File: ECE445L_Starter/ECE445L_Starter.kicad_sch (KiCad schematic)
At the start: 20 parts, among them J101 EXT_3V3, Q101 IRLD024PBF, SW101 UP, SW102 DOWN, SW103 LEFT, SW104 RIGHT, SW105 MODE, U101 EK-TM4C123GXL, U102 ESP8266-1, U103 Adafruit ST7735R

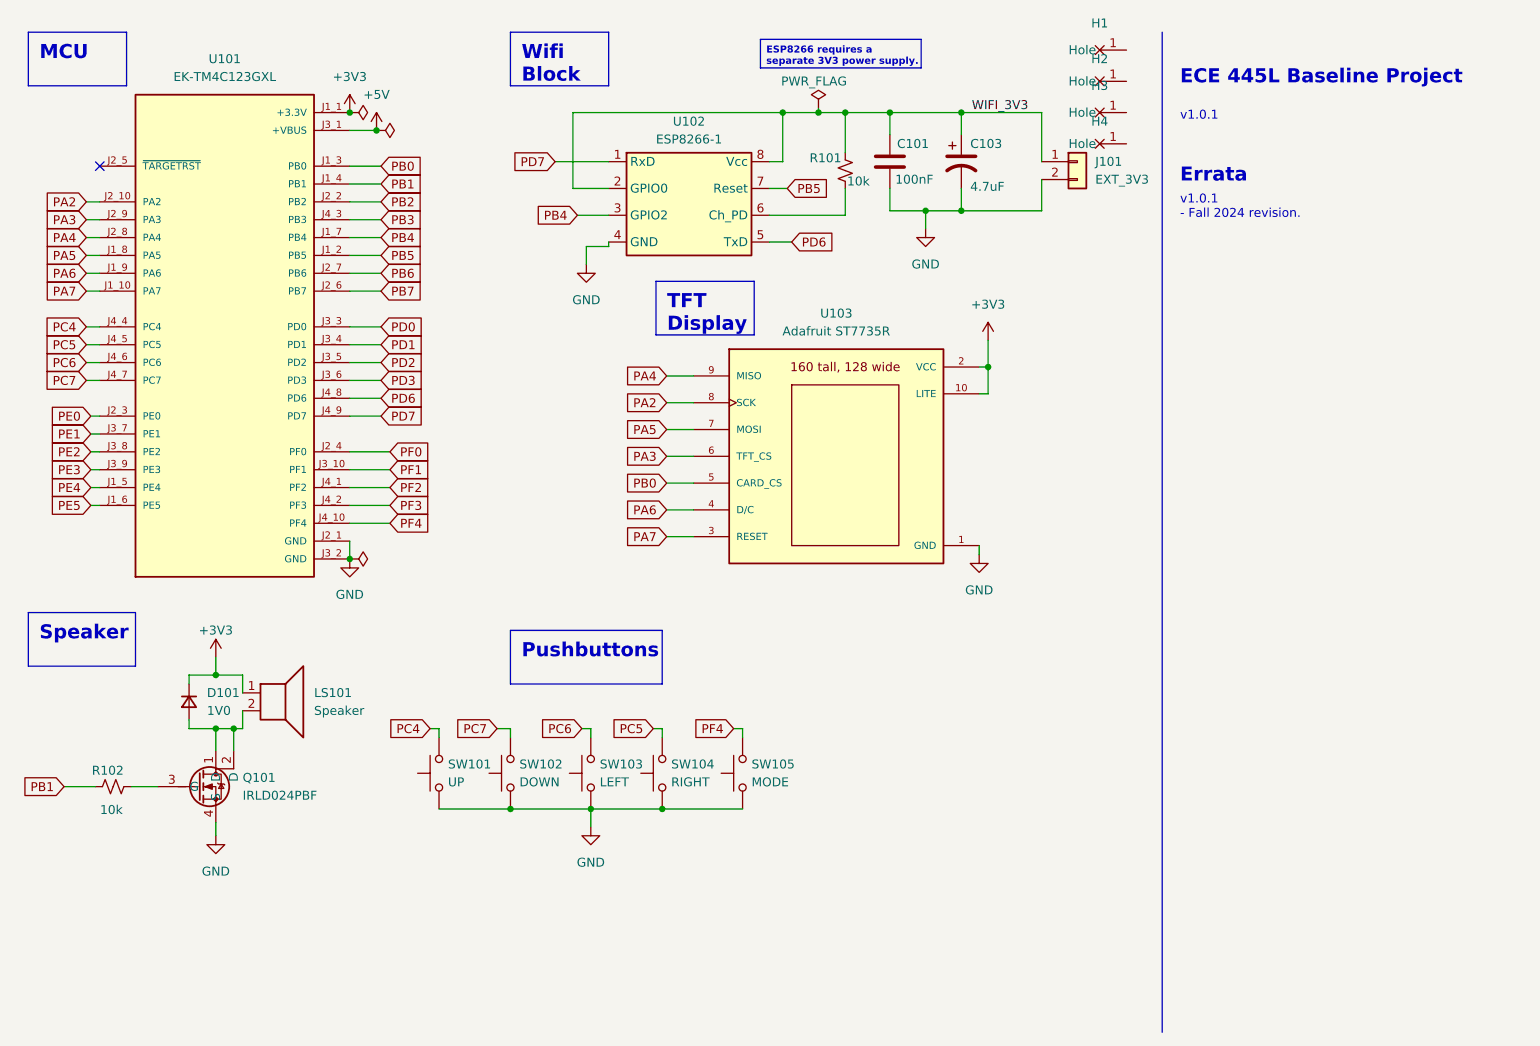
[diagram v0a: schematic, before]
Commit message: update all symbols and re-sync footprints in the KiCad projects
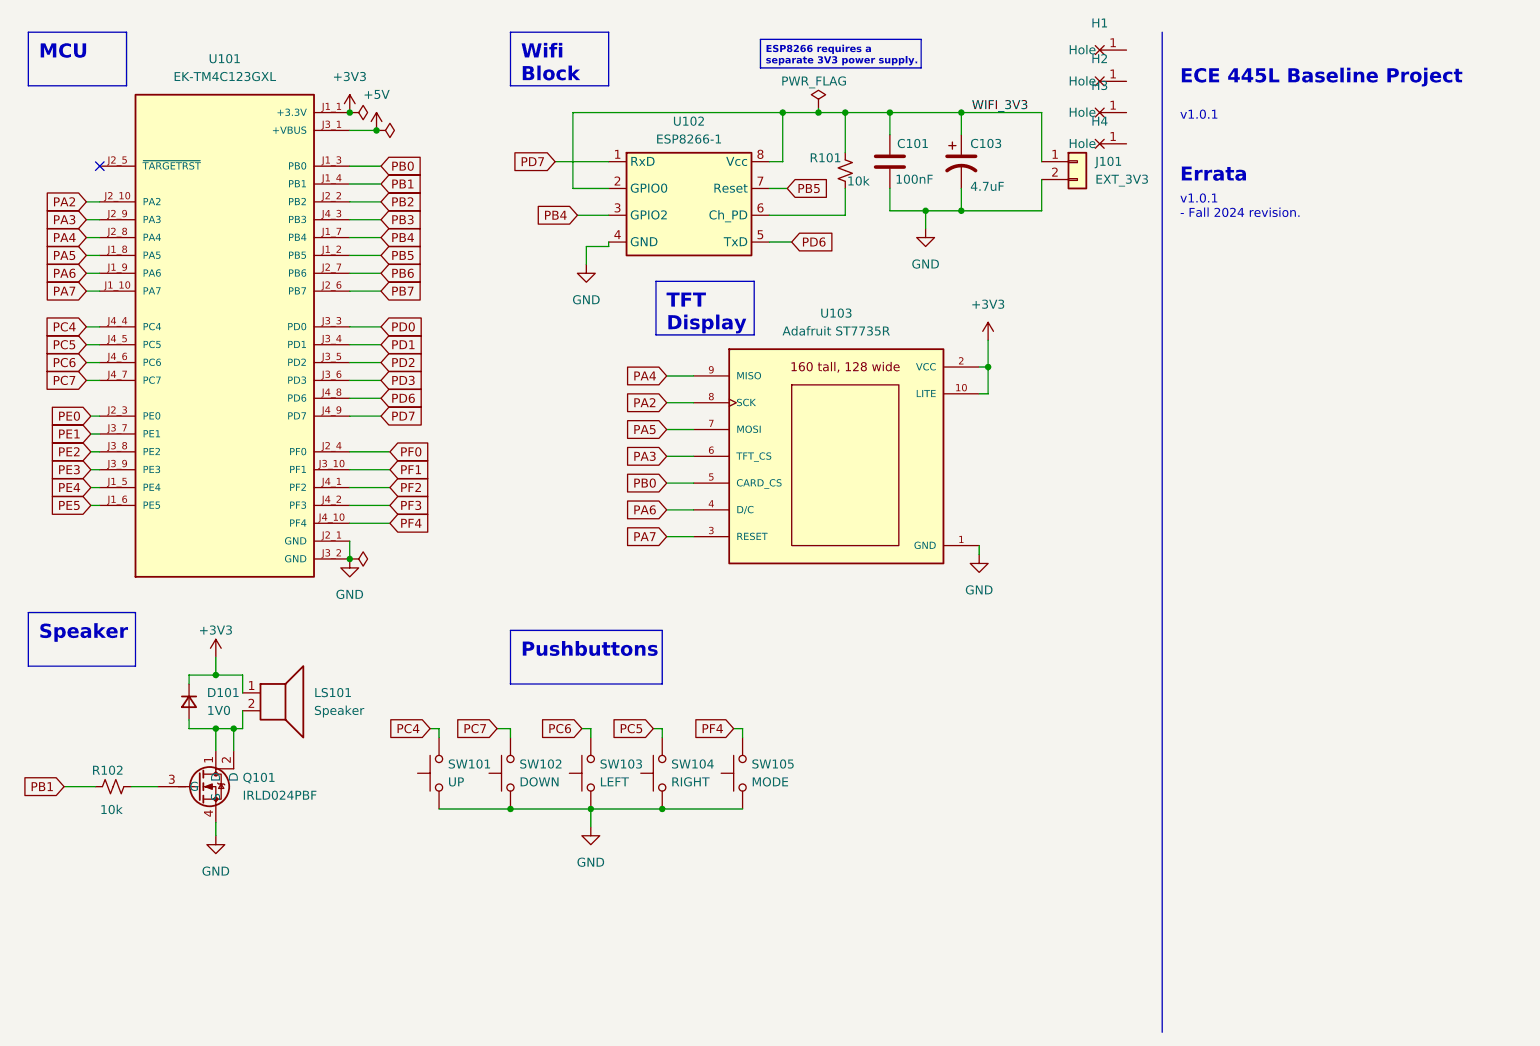
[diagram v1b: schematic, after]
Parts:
- U102: footprint ECE445L:PinHeader_2x04_P2.54mm_Vertical -> ECE445L:ESP8266_FemaleConnector
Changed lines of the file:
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@@
 (kicad_sch
-	(version 20231120)
+	(version 20250114)
 	(generator "eeschema")
-	(generator_version "8.0")
+	(generator_version "9.0")
 	(paper "A4")
 	(title_block
@@
 		(company "The University of Texas at Austin")
 	)
+	(text "v1.0.1\n- Fall 2024 revision."
+		(exclude_from_sim no)
+		(at 179.07 41.91 0)
+		(effects
+			(font
+				(size 1.27 1.27)
+			)
+			(justify left bottom)
+		)
+	)
+	(text "ECE 445L Baseline Project"
+		(exclude_from_sim no)
+		(at 179.07 22.86 0)
+		(effects
+			(font
+				(size 2 2)
+				(thickness 0.6)
+				(bold yes)
+			)
+			(justify left bottom)
+		)
+	)
+	(text "v1.0.1"
+		(exclude_from_sim no)
+		(at 179.07 27.94 0)
+		(effects
+			(font
+				(size 1.27 1.27)
+			)
+			(justify left bottom)
+		)
+	)
+	(text "Errata"
+		(exclude_from_sim no)
+		(at 179.07 36.83 0)
+		(effects
+			(font
+				(size 2 2)
+				(thickness 0.4)
+				(bold yes)
+			)
+			(justify left bottom)
+		)
+	)
+	(text_box "MCU"
+		(exclude_from_sim no)
+		(at 15.24 15.24 0)
+		(size 13.97 7.62)
+		(margins 1.5 1.5 1.5 1.5)
+		(stroke
+			(width 0)
+			(type default)
+		)
+		(fill
+			(type none)
+		)
+		(effects
+			(font
+				(size 2 2)
+				(thickness 0.4)
+				(bold yes)
+			)
+			(justify left top)
+		)
+	)
+	(text_box "ESP8266 requires a separate 3V3 power supply."
+		(exclude_from_sim no)
+		(at 119.38 16.256 0)
+		(size 22.86 4.064)
+		(margins 0.75 0.75 0.75 0.75)
+		(stroke
+			(width 0)
+			(type default)
+		)
+		(fill
+			(type none)
+		)
+		(effects
+			(font
+				(size 1 1)
+				(bold yes)
+			)
+			(justify left top)
+		)
+	)
+	(text_box "Speaker"
+		(exclude_from_sim no)
+		(at 15.24 97.79 0)
+		(size 15.24 7.62)
+		(margins 1.5 1.5 1.5 1.5)
+		(stroke
+			(width 0)
+			(type default)
+		)
+		(fill
+			(type none)
+		)
+		(effects
+			(font
+				(size 2 2)
+				(thickness 0.4)
+				(bold yes)
+			)
+			(justify left top)
+		)
+	)
+	(text_box "Pushbuttons"
+		(exclude_from_sim no)
+		(at 83.82 100.33 0)
+		(size 21.59 7.62)
+		(margins 1.5 1.5 1.5 1.5)
+		(stroke
+			(width 0)
+			(type default)
+		)
+		(fill
+			(type none)
+		)
+		(effects
+			(font
+				(size 2 2)
+				(thickness 0.4)
+				(bold yes)
+			)
+			(justify left top)
+		)
+	)
+	(text_box "TFT Display"
+		(exclude_from_sim no)
+		(at 104.521 50.673 0)
+		(size 13.97 7.62)
+		(margins 1.5 1.5 1.5 1.5)
+		(stroke
+			(width 0)
+			(type default)
+		)
+		(fill
+			(type none)
+		)
+		(effects
+			(font
+				(size 2 2)
+				(thickness 0.4)
+				(bold yes)
+			)
+			(justify left top)
+		)
+	)
+	(text_box "Wifi Block"
+		(exclude_from_sim no)
+		(at 83.82 15.24 0)
+		(size 13.97 7.62)
+		(margins 1.5 1.5 1.5 1.5)
+		(stroke
+			(width 0)
+			(type default)
+		)
+		(fill
+			(type none)
+		)
+		(effects
+			(font
+				(size 2 2)
+				(thickness 0.4)
+				(bold yes)
+			)
+			(justify left top)
+		)
+	)
 	(junction
 		(at 60.96 26.67)
@@
 		)
 	)
-	(text_box "MCU"
-		(exclude_from_sim no)
-		(at 15.24 15.24 0)
-		(size 13.97 7.62)
-		(stroke
-			(width 0)
-			(type default)
-		)
-		(fill
-			(type none)
-		)
-		(effects
-			(font
-				(size 2 2)
-				(thickness 0.4)
-				(bold yes)
-			)
-			(justify left top)
-		)
-	)
-	(text_box "ESP8266 requires a separate 3V3 power supply."
-		(exclude_from_sim no)
-		(at 119.38 16.256 0)
-		(size 22.86 4.064)
-		(stroke
-			(width 0)
-			(type default)
-		)
-		(fill
-			(type none)
-		)
-		(effects
-			(font
-				(size 1 1)
-				(bold yes)
-			)
-			(justify left top)
-		)
-	)
-	(text_box "Speaker"
-		(exclude_from_sim no)
-		(at 15.24 97.79 0)
-		(size 15.24 7.62)
-		(stroke
-			(width 0)
-			(type default)
-		)
-		(fill
-			(type none)
-		)
-		(effects
-			(font
-				(size 2 2)
-				(thickness 0.4)
-				(bold yes)
-			)
-			(justify left top)
-		)
-	)
-	(text_box "Pushbuttons"
-		(exclude_from_sim no)
-		(at 83.82 100.33 0)
-		(size 21.59 7.62)
-		(stroke
-			(width 0)
-			(type default)
-		)
-		(fill
-			(type none)
-		)
-		(effects
-			(font
-				(size 2 2)
-				(thickness 0.4)
-				(bold yes)
-			)
-			(justify left top)
-		)
-	)
-	(text_box "TFT Display"
-		(exclude_from_sim no)
-		(at 104.521 50.673 0)
-		(size 13.97 7.62)
-		(stroke
-			(width 0)
-			(type default)
-		)
-		(fill
-			(type none)
-		)
-		(effects
-			(font
-				(size 2 2)
-				(thickness 0.4)
-				(bold yes)
-			)
-			(justify left top)
-		)
-	)
-	(text_box "Wifi Block"
-		(exclude_from_sim no)
-		(at 83.82 15.24 0)
-		(size 13.97 7.62)
-		(stroke
-			(width 0)
-			(type default)
-		)
-		(fill
-			(type none)
-		)
-		(effects
-			(font
-				(size 2 2)
-				(thickness 0.4)
-				(bold yes)
-			)
-			(justify left top)
-		)
-	)
-	(text "v1.0.1\n- Fall 2024 revision."
-		(exclude_from_sim no)
-		(at 179.07 41.91 0)
-		(effects
-			(font
-				(size 1.27 1.27)
-			)
-			(justify left bottom)
-		)
-	)
-	(text "ECE 445L Baseline Project"
-		(exclude_from_sim no)
-		(at 179.07 22.86 0)
-		(effects
-			(font
-				(size 2 2)
-				(thickness 0.6)
-				(bold yes)
-			)
-			(justify left bottom)
-		)
-	)
-	(text "v1.0.1"
-		(exclude_from_sim no)
-		(at 179.07 27.94 0)
-		(effects
-			(font
-				(size 1.27 1.27)
-			)
-			(justify left bottom)
-		)
-	)
-	(text "Errata"
-		(exclude_from_sim no)
-		(at 179.07 36.83 0)
-		(effects
-			(font
-				(size 2 2)
-				(thickness 0.4)
-				(bold yes)
-			)
-			(justify left bottom)
-		)
-	)
 	(label "WIFI_3V3"
 		(at 157.48 26.67 180)
-		(fields_autoplaced yes)
 		(effects
 			(font
@@
 			)
 		)
-		(property "Footprint" "ECE445L:PinHeader_2x04_P2.54mm_Vertical"
+		(property "Footprint" "ECE445L:ESP8266_FemaleConnector"
 			(at 108.585 46.99 0)
 			(effects
@@
 		)
 	)
+	(embedded_fonts no)
 )
